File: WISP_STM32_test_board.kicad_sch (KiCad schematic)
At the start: 30 parts, among them J1 Conn_02x05_Odd_Even, J2 Conn_02x01, J3 Conn_02x01, J5 Conn_01x02_Pin, J6 Conn_01x09_Pin, U1 MAX3072E, U2 MAX3072E, U3 AMS1117-3.3, U4 STM32F446RETx

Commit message: Full 15 rough draft
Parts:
- removed J6: Conn_01x09_Pin, Connector_PinSocket_2.54mm:PinSocket_1x09_P2.54mm_Vertical, symbol Connector:Conn_01x09_Pin
- added J4: Conn_01x10_Pin, symbol Connector:Conn_01x10_Pin
- added R4, R5: 10K, Resistor_SMD:R_0805_2012Metric_Pad1.20x1.40mm_HandSolder, symbol Device:R
- added SW1, SW2: SW_Push, Button_Switch_THT:SW_PUSH_6mm, symbol Switch:SW_Push
- added SW3: SW_SPST, symbol Switch:SW_SPST
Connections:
- net +3.3V: now also J4.1 (Pin_1)
- net GND: now also J4.2 (Pin_2), SW1.2, SW2.2
- net I2C1_SCL: now also J4.7 (Pin_7)
- net I2C1_SDA: now also J4.6 (Pin_6)
- net SPI3_MOSI: now also J4.8 (Pin_8)
- net SPI3_SCK: now also J4.9 (Pin_9)
- net SPI3_STCP: now also J4.10 (Pin_10)
- net at F1.2: now also SW3.1 (A); no longer FB1.1
- net CTRL_1: now reaches U4.27 (PB1)
- net CTRL_1: now also R4.1
- net CTRL_2: now reaches U4.33 (PB12)
- net CTRL_2: now also R5.1
- net I2C_AD1: now reaches U4.37 (PC6)
- net I2C_AD1: now also J4.4 (Pin_4)
- net I2C_AD2: now reaches U4.53 (PC12)
- net I2C_AD2: now also J4.5 (Pin_5)
- net I2C_AD0: now reaches U4.9 (PC1)
- net I2C_AD0: now also J4.3 (Pin_3)
- net I2C3_SCL: no longer names the net of U4.41 (PA8)
- net I2C3_SDA: no longer names the net of U4.40 (PC9)
- new net: R5.2, SW2.1
- new net: R4.2, SW1.1
- new net: FB1.1, SW3.2 (B)
- no-connect marks 36 -> 33
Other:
- note added: "Panel Control"
- company: (none) -> Wisconsin Space Program
- title: (none) -> P&ID display control board
- moved on the sheet: C12, C13, J2, J3, U1, U2

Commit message: V1 routing
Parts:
- J4: footprint (none) -> Connector_JST:JST_XH_B10B-XH-A_1x10_P2.50mm_Vertical
- SW3: footprint (none) -> Button_Switch_SMD:SW_DIP_SPSTx01_Slide_6.7x4.1mm_W6.73mm_P2.54mm_LowProfile_JPin
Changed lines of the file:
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@@
 			)
 		)
-		(property "Footprint" ""
+		(property "Footprint" "Button_Switch_SMD:SW_DIP_SPSTx01_Slide_6.7x4.1mm_W6.73mm_P2.54mm_LowProfile_JPin"
 			(at 41.91 40.64 0)
 			(effects
@@
 			)
 		)
-		(property "Footprint" ""
+		(property "Footprint" "Connector_JST:JST_XH_B10B-XH-A_1x10_P2.50mm_Vertical"
 			(at 234.95 31.75 0)
 			(effects

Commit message: Rough draft V2
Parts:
- removed C1, C2: 10uF, Capacitor_SMD:C_0805_2012Metric_Pad1.18x1.45mm_HandSolder, symbol Device:C
- removed D1: B5819W, Diode_SMD:D_SOD-123, symbol Device:D_Schottky_Small
- removed D3: Red, LED_SMD:LED_0805_2012Metric_Pad1.15x1.40mm_HandSolder, symbol Device:LED_Small
- removed F1: 500mA, Fuse:Fuse_0805_2012Metric_Pad1.15x1.40mm_HandSolder, symbol Device:Fuse_Small
- removed FB1: 100 @ 100MHz, Resistor_SMD:R_0805_2012Metric_Pad1.20x1.40mm_HandSolder, symbol Device:FerriteBead_Small
- removed R3: 2k2, Resistor_SMD:R_0805_2012Metric_Pad1.20x1.40mm_HandSolder, symbol Device:R
- removed SW3: SW_SPST, Button_Switch_SMD:SW_DIP_SPSTx01_Slide_6.7x4.1mm_W6.73mm_P2.54mm_LowProfile_JPin, symbol Switch:SW_SPST
- removed U3: AMS1117-3.3, Package_TO_SOT_SMD:SOT-223-3_TabPin2, symbol Regulator_Linear:AMS1117-3.3
- added C16: 10uF, Capacitor_SMD:C_0805_2012Metric_Pad1.18x1.45mm_HandSolder, symbol Device:C_Small
- added C17: 100nF, Capacitor_SMD:C_0805_2012Metric_Pad1.18x1.45mm_HandSolder, symbol Device:C_Small
- added C18, C19: 22uF, Capacitor_SMD:C_0805_2012Metric_Pad1.18x1.45mm_HandSolder, symbol Device:C_Small
- added D5: Red, LED_SMD:LED_0805_2012Metric_Pad1.15x1.40mm_HandSolder, symbol Device:LED_Small
- added L2: 2.2uH, Inductor_SMD:L_0805_2012Metric_Pad1.05x1.20mm_HandSolder, symbol Device:L
- added R6, R7: 120, Resistor_SMD:R_0805_2012Metric_Pad1.20x1.40mm_HandSolder, symbol Device:R_Small
- added R9: 2k2, Resistor_SMD:R_0805_2012Metric_Pad1.20x1.40mm_HandSolder, symbol Device:R
- added SW5: SW_SPST, Button_Switch_THT:SW_CK_JS202011CQN_DPDT_Straight, symbol Switch:SW_SPST
- added U6: AP63203WU, Package_TO_SOT_SMD:TSOT-23-6, symbol Regulator_Switching:AP63203WU
- J1: footprint Connector_PinSocket_2.54mm:PinSocket_2x05_P2.54mm_Vertical -> Connector_PinHeader_2.54mm:PinHeader_2x05_P2.54mm_Vertical
- J2, J3: footprint Connector_PinSocket_2.54mm:PinSocket_1x02_P2.54mm_Vertical -> TerminalBlock:TerminalBlock_Xinya_XY308-2.54-2P_1x02_P2.54mm_Horizontal
- J4: footprint Connector_JST:JST_XH_B10B-XH-A_1x10_P2.50mm_Vertical -> Connector_PinHeader_2.54mm:PinHeader_1x10_P2.54mm_Vertical
- J5: footprint Connector_JST:JST_PH_B2B-PH-K_1x02_P2.00mm_Vertical -> Connector_PinSocket_2.54mm:PinSocket_1x02_P2.54mm_Vertical
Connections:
- net +3.3V: now also C18.2, D5.2 (A), L2.2, U6.1 (FB)
- net GND: now also C16.1, C19.1, R9.1, U6.4 (GND)
- net VCC: now also SW5.1 (A)
- net at J2.1 (Pin_1), U2.6 (A): now also R6.1
- net at J2.2 (Pin_2), U2.7 (B): now also R6.2
- net at J3.1 (Pin_1), U1.6 (A): now also R7.1
- net at J3.2 (Pin_2), U1.7 (B): now also R7.2
- new net: C18.1, C19.2
- new net: D5.1 (K), R9.2
- new net: C16.2, SW5.2 (B), U6.2 (EN), U6.3 (IN)
- new net: C17.2, U6.5 (SW)
- new net: C17.1, L2.1, U6.6 (BST)

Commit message: John revisions 9/7
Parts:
- removed J2, J3: Conn_02x01, TerminalBlock:TerminalBlock_Xinya_XY308-2.54-2P_1x02_P2.54mm_Horizontal, symbol Connector_Generic:Conn_02x01
- added J6, J7: Conn_01x03_Socket, TerminalBlock:TerminalBlock_Xinya_XY308-2.54-3P_1x03_P2.54mm_Horizontal, symbol Connector:Conn_01x03_Socket
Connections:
- net GND: now also J6.1 (Pin_1), J7.1 (Pin_1)
- net at R6.1, U2.6 (A): now also J6.2 (Pin_2)
- net at R6.2, U2.7 (B): now also J6.3 (Pin_3)
- net at R7.1, U1.6 (A): now also J7.2 (Pin_2)
- net at R7.2, U1.7 (B): now also J7.3 (Pin_3)

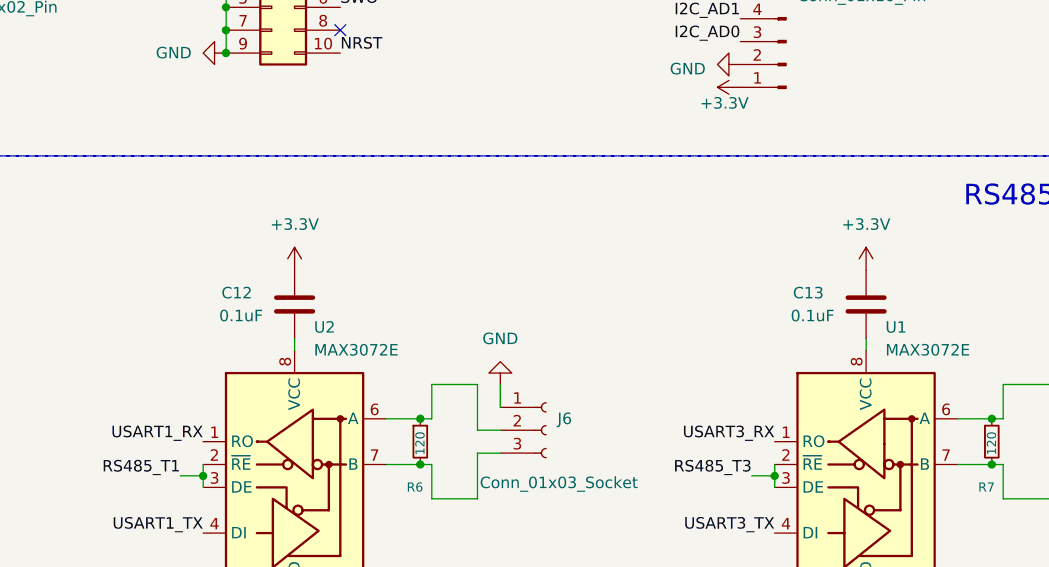
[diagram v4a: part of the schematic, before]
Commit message: Fixed decoupling capacitors
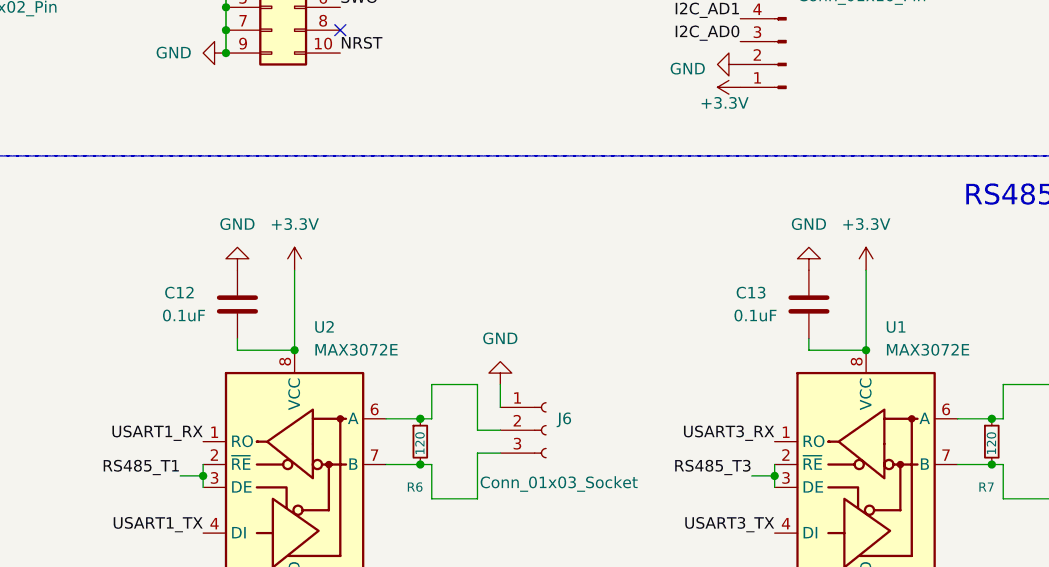
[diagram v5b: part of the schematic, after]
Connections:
- net +3.3V: now also C12.2, C13.2, U1.8 (VCC), U2.8 (VCC); no longer C12.1, C13.1
- net GND: now also C12.1, C13.1
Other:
- moved on the sheet: C12, C13
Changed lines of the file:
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@@
 	)
 	(junction
+		(at 243.84 71.12)
+		(diameter 0)
+		(color 0 0 0 0)
+	)
+	(junction
 		(at 104.14 73.66)
 		(diameter 0)
@@
 	)
 	(junction
+		(at 180.34 71.12)
+		(diameter 0)
+		(color 0 0 0 0)
+	)
+	(junction
 		(at 172.72 35.56)
 		(diameter 0)
@@
 	(wire
 		(pts
-			(xy 243.84 69.85) (xy 243.84 71.12)
+			(xy 237.49 69.85) (xy 237.49 71.12)
 		)
 		(stroke
@@
 	(wire
 		(pts
+			(xy 173.99 71.12) (xy 180.34 71.12)
+		)
+		(stroke
+			(width 0)
+			(type default)
+		)
+	)
+	(wire
+		(pts
 			(xy 52.07 87.63) (xy 54.61 87.63)
 		)
@@
 	(wire
 		(pts
+			(xy 237.49 71.12) (xy 243.84 71.12)
+		)
+		(stroke
+			(width 0)
+			(type default)
+		)
+	)
+	(wire
+		(pts
 			(xy 254 83.82) (xy 257.81 83.82)
 		)
@@
 	(wire
 		(pts
+			(xy 243.84 62.23) (xy 243.84 71.12)
+		)
+		(stroke
+			(width 0)
+			(type default)
+		)
+	)
+	(wire
+		(pts
 			(xy 44.45 87.63) (xy 46.99 87.63)
 		)
@@
 	(wire
 		(pts
+			(xy 180.34 62.23) (xy 180.34 71.12)
+		)
+		(stroke
+			(width 0)
+			(type default)
+		)
+	)
+	(wire
+		(pts
 			(xy 231.14 85.09) (xy 233.68 85.09)
 		)
@@
 	(wire
 		(pts
-			(xy 180.34 69.85) (xy 180.34 71.12)
+			(xy 173.99 69.85) (xy 173.99 71.12)
 		)
 		(stroke
@@
 	(symbol
 		(lib_id "Device:C")
-		(at 180.34 66.04 0)
+		(at 173.99 66.04 0)
 		(unit 1)
 		(exclude_from_sim no)
@@
 		(dnp no)
 		(property "Reference" "C12"
-			(at 172.212 64.77 0)
+			(at 165.862 64.77 0)
 			(effects
 				(font
@@
 		)
 		(property "Value" "0.1uF"
-			(at 171.958 67.31 0)
+			(at 165.608 67.31 0)
 			(effects
 				(font
@@
 		)
 		(property "Footprint" "Capacitor_SMD:C_0805_2012Metric_Pad1.18x1.45mm_HandSolder"
-			(at 181.3052 69.85 0)
+			(at 174.9552 69.85 0)
 			(effects
 				(font
@@
 		)
 		(property "Datasheet" "~"
-			(at 180.34 66.04 0)
+			(at 173.99 66.04 0)
 			(effects
 				(font
@@
 		)
 		(property "Description" "Unpolarized capacitor"
-			(at 180.34 66.04 0)
+			(at 173.99 66.04 0)
 			(effects
 				(font
@@
 	)
 	(symbol
+		(lib_id "power:GND")
+		(at 173.99 62.23 180)
+		(unit 1)
+		(exclude_from_sim no)
+		(in_bom yes)
+		(on_board yes)
+		(dnp no)
+		(fields_autoplaced yes)
+		(property "Reference" "#PWR016"
+			(at 173.99 55.88 0)
+			(effects
+				(font
+					(size 1.27 1.27)
+				)
+				(hide yes)
+			)
+		)
+		(property "Value" "GND"
+			(at 173.99 57.15 0)
+			(effects
+				(font
+					(size 1.27 1.27)
+				)
+			)
+		)
+		(property "Footprint" ""
+			(at 173.99 62.23 0)
+			(effects
+				(font
+					(size 1.27 1.27)
+				)
+				(hide yes)
+			)
+		)
+		(property "Datasheet" ""
+			(at 173.99 62.23 0)
+			(effects
+				(font
+					(size 1.27 1.27)
+				)
+				(hide yes)
+			)
+		)
+		(property "Description" "Power symbol creates a global label with name \"GND\" , ground"
+			(at 173.99 62.23 0)
+			(effects
+				(font
+					(size 1.27 1.27)
+				)
+				(hide yes)
+			)
+		)
+		(pin "1"
+		)
+		(instances
+			(project ""
+				(path "/bbf92a7f-e2a8-4909-aabd-f6b15409995d"
+					(reference "#PWR016")
+					(unit 1)
+				)
+			)
+		)
+	)
+	(symbol
 		(lib_id "Device:C")
-		(at 243.84 66.04 0)
+		(at 237.49 66.04 0)
 		(unit 1)
 		(exclude_from_sim no)
@@
 		(dnp no)
 		(property "Reference" "C13"
-			(at 235.712 64.77 0)
+			(at 229.362 64.77 0)
 			(effects
 				(font
@@
 		)
 		(property "Value" "0.1uF"
-			(at 235.458 67.31 0)
+			(at 229.108 67.31 0)
 			(effects
 				(font
@@
 		)
 		(property "Footprint" "Capacitor_SMD:C_0805_2012Metric_Pad1.18x1.45mm_HandSolder"
-			(at 244.8052 69.85 0)
+			(at 238.4552 69.85 0)
 			(effects
 				(font
@@
 		)
 		(property "Datasheet" "~"
-			(at 243.84 66.04 0)
+			(at 237.49 66.04 0)
 			(effects
 				(font
@@
 		)
 		(property "Description" "Unpolarized capacitor"
-			(at 243.84 66.04 0)
+			(at 237.49 66.04 0)
 			(effects
 				(font
@@
 					(unit 1)
 				)
+			)
+		)
+	)
+	(symbol
+		(lib_id "power:GND")
+		(at 237.49 62.23 180)
+		(unit 1)
+		(exclude_from_sim no)
+		(in_bom yes)
+		(on_board yes)
+		(dnp no)
+		(fields_autoplaced yes)
+		(property "Reference" "#PWR018"
+			(at 237.49 55.88 0)
+			(effects
+				(font
+					(size 1.27 1.27)
+				)
+				(hide yes)
+			)
+		)
+		(property "Value" "GND"
+			(at 237.49 57.15 0)
+			(effects
+				(font
+					(size 1.27 1.27)
+				)
+			)
+		)
+		(property "Footprint" ""
+			(at 237.49 62.23 0)
+			(effects
+				(font
+					(size 1.27 1.27)
+				)
+				(hide yes)
+			)
+		)
+		(property "Datasheet" ""
+			(at 237.49 62.23 0)
+			(effects
+				(font
+					(size 1.27 1.27)
+				)
+				(hide yes)
+			)
+		)
+		(property "Description" "Power symbol creates a global label with name \"GND\" , ground"
+			(at 237.49 62.23 0)
+			(effects
+				(font
+					(size 1.27 1.27)
+				)
+				(hide yes)
+			)
+		)
+		(pin "1"
+		)
+		(instances
+			(project ""
+				(path "/bbf92a7f-e2a8-4909-aabd-f6b15409995d"
+					(reference "#PWR018")
+					(unit 1)
+				)

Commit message: Rough draft V3
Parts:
- added H1, H2, H3, H4: MountingHole, MountingHole:MountingHole_2.2mm_M2, symbol Mechanical:MountingHole
- added TP1: 3.3V, TestPoint:TestPoint_Pad_1.0x1.0mm, symbol Connector:TestPoint
- added TP2: GND, TestPoint:TestPoint_Pad_1.0x1.0mm, symbol Connector:TestPoint
- L2: value 2.2uH -> 4.7uH
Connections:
- net +3.3V: now also TP1.1
- net GND: now also TP2.1
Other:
- moved on the sheet: C17

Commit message: Rough draft V4
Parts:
- removed C10, C7, C8, C9: 100nF, Capacitor_SMD:C_0805_2012Metric_Pad1.18x1.45mm_HandSolder, symbol Device:C
- added C1: 100nF, Capacitor_SMD:C_0603_1608Metric, symbol Device:C
- C11, C3, C4, C5, C6: footprint Capacitor_SMD:C_0805_2012Metric_Pad1.18x1.45mm_HandSolder -> Capacitor_SMD:C_0603_1608Metric
- L2: footprint Inductor_SMD:L_0805_2012Metric_Pad1.05x1.20mm_HandSolder -> Inductor_SMD:L_Taiyo-Yuden_MD-4040
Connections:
- net +3.3V: now also C1.1
- net GND: now also C1.2
- net at U6.5 (SW): now also C17.1, L2.1; no longer C17.2
- new net: C17.2, U6.6 (BST)
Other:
- moved on the sheet: C11, C17, C3, C4, C5, C6
